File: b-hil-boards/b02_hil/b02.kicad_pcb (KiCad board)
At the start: 2 copper layers, 100 x 50 mm, 52 parts, among them J1 Conn_01x12_Socket, J2 Conn_01x06_Socket, K1 Relay_DPDT, K2 Relay_DPDT, K3 Relay_DPDT, K4 Relay_DPDT, SW1 SW_Push, U1 MAX485E, U2 ULN2003, U3 ADuM1412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

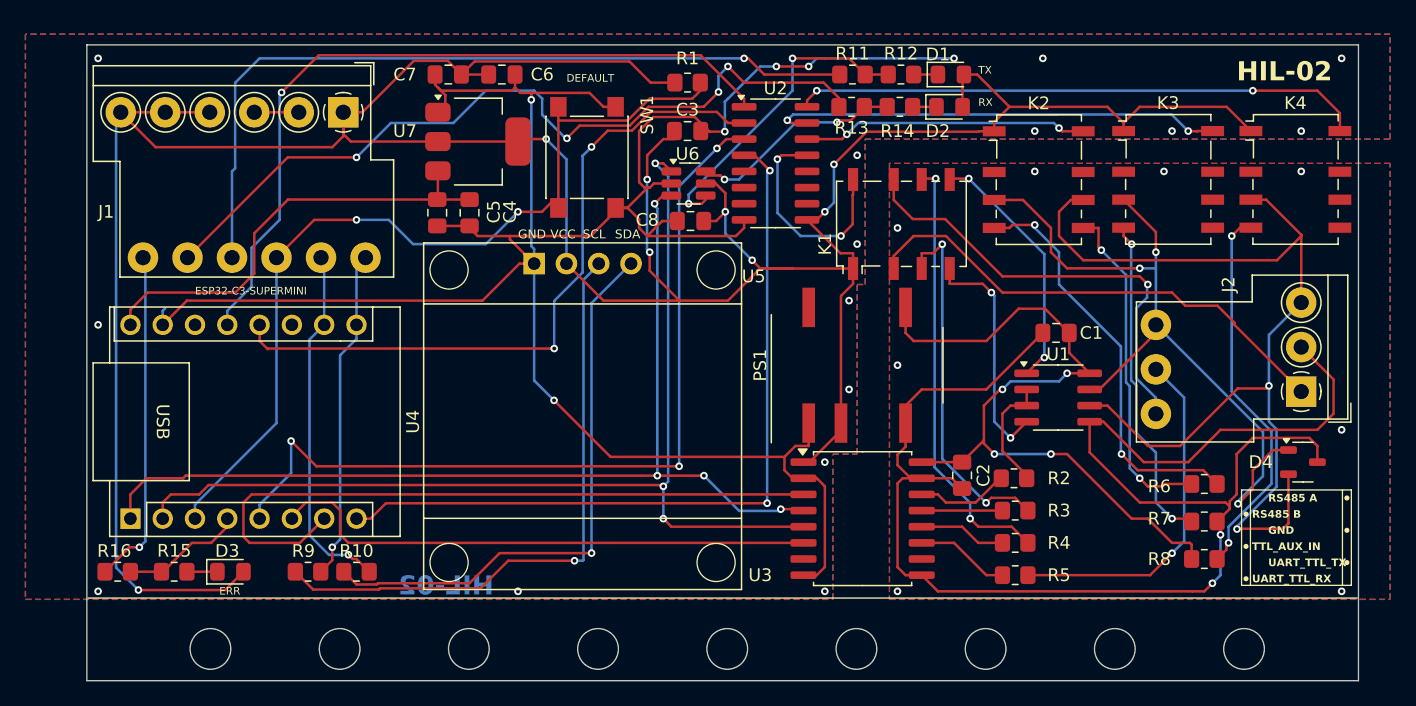
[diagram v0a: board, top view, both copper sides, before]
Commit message: B02: add tri-state buffer and re-route PCB
Add 74HCT541 tri-state buffer to the schematic and re-route b02.kicad_pcb
to integrate the new device. Update project layout, refresh FreeRouting
exchange files (b02.dsn, b02.rules, b02.ses), and rotate KiCad automatic
backup archives.
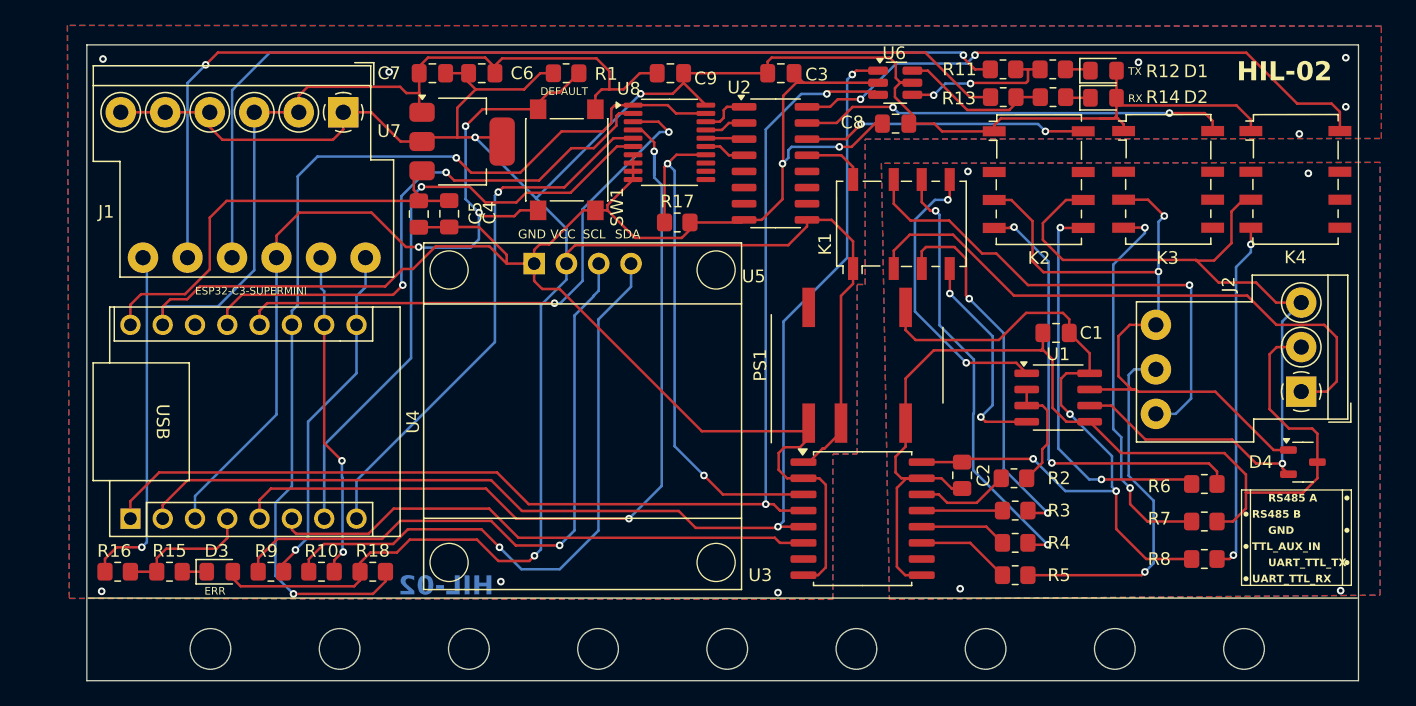
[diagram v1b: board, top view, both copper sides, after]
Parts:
- added C9: C, Capacitor_SMD:C_0805_2012Metric_Pad1.18x1.45mm_HandSolder, F.Cu at (125.6, 36.7)
- added R17: R, Resistor_SMD:R_0805_2012Metric_Pad1.20x1.40mm_HandSolder, F.Cu at (126.2, 48.5)
- added R18: R, Resistor_SMD:R_0805_2012Metric_Pad1.20x1.40mm_HandSolder, F.Cu at (102.2, 75.9)
- added U8: 74HCT541, Package_SO:TSSOP-20_4.4x6.5mm_P0.65mm, F.Cu at (125.6, 42.2)
- moved U6 18.1 mm to (143.3, 37.5)
- moved C8 17.9 mm to (143.4, 40.7)
- moved D2 12.1 mm to (159.7, 38.7)
- moved R14 12.1 mm to (155.7, 38.6)
- moved D1 12.0 mm to (159.7, 36.5)
- moved R13 11.9 mm to (151.8, 38.6)
- moved R12 11.9 mm to (155.7, 36.4)
- moved R11 11.8 mm to (151.8, 36.4)
- moved R1 9.58 mm to (117.4, 36.7)
- moved C3 8.63 mm to (134.3, 36.7)
- moved R9 2.92 mm to (94.2, 75.9)
- moved R10 2.75 mm to (98.2, 75.9)
- moved C4 1.60 mm to (108.3, 47.8)
- moved SW1 1.60 mm to (117.5, 43.5)
- moved C6 1.58 mm to (110.8, 36.7)
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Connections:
- U3 pad 3: /485_CTR -> /485_DRV
- U4 pad 11: unconnected-(U4-GPIO2-Pad11) -> //KOE
- U4 pad 12: Net-(U2-I2) -> Net-(U4-GPIO3)
- U4 pad 13: Net-(U2-I1) -> Net-(U4-GPIO4)
- U4 pad 5: Net-(U2-I3) -> Net-(U4-GPIO9)
- U4 pad 8: Net-(U2-I4) -> Net-(U4-GPIO21)
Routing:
- net //KOE: track 0.00 -> 78.9 mm, vias 0 -> 2
- net Net-(U4-GPIO9): track 0.00 -> 66.7 mm, vias 0 -> 2
- net Net-(U2-I3): track 67.1 -> 3.03 mm, vias 3 -> 0
- net Net-(U2-I4): track 61.6 -> 3.29 mm, vias 2 -> 0
- net Net-(U2-I1): track 59.7 -> 3.85 mm, vias 1 -> 0
- net Net-(U2-I2): track 55.3 -> 3.23 mm, vias 2 -> 0
- net Net-(U4-GPIO3): track 0.00 -> 45.6 mm, vias 0 -> 2
- net Net-(U4-GPIO4): track 0.00 -> 44.7 mm, vias 0 -> 2
- net Net-(U4-GPIO21): track 0.00 -> 42.7 mm, vias 0 -> 1
- net /485_DRV: track 0.00 -> 42.2 mm, vias 0 -> 2
- net GND2: track 121.5 -> 85.7 mm, vias 10 -> 4
- net +3V3: track 262.0 -> 237.6 mm, vias 8 -> 3
- net GND1: track 191.1 -> 209.9 mm, vias 21 -> 11
- net /TX: track 79.5 -> 96.1 mm, vias 4 -> 2
- net /RX_LED_EXT: track 63.8 -> 79.3 mm, vias 4 -> 1
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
